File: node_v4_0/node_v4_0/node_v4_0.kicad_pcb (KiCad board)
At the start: 4 copper layers, 45.7 x 76.2 mm, 51 parts, among them J1 Conn_01x02_Pin, J2 12402012E212A, Q1 DMG2301L, U1 RP2040, U2 W25Q128JVS, U3 AP2112K-3.3, U4 CAT3200-5, U5 MCP73831-2-OT, U6 RFM69HCW, U7 PTS526 SK15 SMTR2 LFS, U8 PTS526 SK15 SMTR2 LFS

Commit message: minor
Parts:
- moved Q1 26.1 mm to (136.6, 85.9), turned to 180 degrees
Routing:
- net +BATT: track 50.3 -> 56.6 mm, vias 1 -> 2
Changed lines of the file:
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@@
 		(at 116.701 53.543 180)
 		(property "Reference" "J2"
-			(at -1.62 -8.405 360)
+			(at -1.62 -8.405 0)
 			(layer "F.SilkS")
 			(effects
@@
 		)
 		(property "Value" "12402012E212A"
-			(at 9.175 -6.715 360)
+			(at 9.175 -6.715 0)
 			(layer "F.Fab")
 			(effects
@@
 		)
 		(property "Footprint" "usbc:AMPHENOL_12402012E212A"
-			(at 0 0 360)
+			(at 0 0 0)
 			(layer "F.Fab")
 			(hide yes)
@@
 		)
 		(property "Datasheet" ""
-			(at 0 0 360)
+			(at 0 0 0)
 			(layer "F.Fab")
 			(hide yes)
@@
 		)
 		(property "Description" ""
-			(at 0 0 360)
+			(at 0 0 0)
 			(layer "F.Fab")
 			(hide yes)
@@
 		(tags "resistor handsolder")
 		(property "Reference" "R7"
-			(at 0 -1.65 360)
+			(at 0 -1.65 0)
 			(layer "F.SilkS")
 			(hide yes)
@@
 		)
 		(property "Value" "R"
-			(at 0 1.65 360)
+			(at 0 1.65 0)
 			(layer "F.Fab")
 			(effects
@@
 		)
 		(fp_text user "${REFERENCE}"
-			(at 0 0 360)
+			(at 0 0 0)
 			(layer "F.Fab")
 			(effects
@@
 	(footprint "Package_TO_SOT_SMD:SOT-23"
 		(layer "F.Cu")
-		(at 160.0985 74.676)
+		(at 136.5735 85.918 180)
 		(descr "SOT, 3 Pin (https://www.jedec.org/system/files/docs/to-236h.pdf variant AB), generated with kicad-footprint-generator ipc_gullwing_generator.py")
 		(tags "SOT TO_SOT_SMD")
 		(property "Reference" "Q1"
-			(at 0 -2.4 0)
+			(at 0 -2.4 360)
 			(layer "F.SilkS")
 			(effects
@@
 		)
 		(property "Value" "DMG2301L"
-			(at 0 2.4 0)
+			(at 0 2.4 360)
 			(layer "F.Fab")
 			(effects
@@
 		)
 		(property "Footprint" "Package_TO_SOT_SMD:SOT-23"
-			(at 0 0 0)
+			(at 0 0 180)
 			(unlocked yes)
 			(layer "F.Fab")
@@
 		)
 		(property "Datasheet" "https://www.diodes.com/assets/Datasheets/DMG2301L.pdf"
-			(at 0 0 0)
+			(at 0 0 180)
 			(unlocked yes)
 			(layer "F.Fab")
@@
 		)
 		(property "Description" "-3A Id, -20V Vds, P-Channel MOSFET, SOT-23"
-			(at 0 0 0)
+			(at 0 0 180)
 			(unlocked yes)
 			(layer "F.Fab")
@@
 		(attr smd)
 		(fp_line
-			(start 0 -1.56)
-			(end -0.65 -1.56)
+			(start 0 1.56)
+			(end 0.65 1.56)
 			(stroke
 				(width 0.12)
@@
 		)
 		(fp_line
-			(start 0 -1.56)
-			(end 0.65 -1.56)
+			(start 0 1.56)
+			(end -0.65 1.56)
 			(stroke
 				(width 0.12)
@@
 		)
 		(fp_line
-			(start 0 1.56)
-			(end -0.65 1.56)
+			(start 0 -1.56)
+			(end 0.65 -1.56)
 			(stroke
 				(width 0.12)
@@
 		)
 		(fp_line
-			(start 0 1.56)
-			(end 0.65 1.56)
+			(start 0 -1.56)
+			(end -0.65 -1.56)
 			(stroke
 				(width 0.12)
@@
 		)
 		(fp_line
-			(start -1.92 -1.7)
-			(end -1.92 1.7)
+			(start 1.92 1.7)
+			(end 1.92 -1.7)
 			(stroke
 				(width 0.05)
@@
 		)
 		(fp_line
-			(start -1.92 1.7)
-			(end 1.92 1.7)
+			(start 1.92 -1.7)
+			(end -1.92 -1.7)
 			(stroke
 				(width 0.05)
@@
 		)
 		(fp_line
-			(start 1.92 -1.7)
-			(end -1.92 -1.7)
+			(start -1.92 1.7)
+			(end 1.92 1.7)
 			(stroke
 				(width 0.05)
@@
 		)
 		(fp_line
-			(start 1.92 1.7)
-			(end 1.92 -1.7)
+			(start -1.92 -1.7)
+			(end -1.92 1.7)
 			(stroke
 				(width 0.05)
@@
 		)
 		(fp_line
-			(start -0.65 -1.125)
-			(end -0.325 -1.45)
+			(start 0.65 1.45)
+			(end -0.65 1.45)
 			(stroke
 				(width 0.1)
@@
 		)
 		(fp_line
-			(start -0.65 1.45)
-			(end -0.65 -1.125)
+			(start 0.65 -1.45)
+			(end 0.65 1.45)
 			(stroke
 				(width 0.1)
@@
 		)
 		(fp_line
-			(start 0.65 -1.45)
-			(end 0.65 1.45)
+			(start -0.65 1.45)
+			(end -0.65 -1.125)
 			(stroke
 				(width 0.1)
@@
 		)
 		(fp_line
-			(start 0.65 1.45)
-			(end -0.65 1.45)
+			(start -0.65 -1.125)
+			(end -0.325 -1.45)
 			(stroke
 				(width 0.1)
@@
 		)
 		(fp_text user "${REFERENCE}"
-			(at 0 0 0)
+			(at 0 0 360)
 			(layer "F.Fab")
 			(effects
@@
 		)
 		(pad "1" smd roundrect
-			(at -0.9375 -0.95)
+			(at -0.9375 -0.95 180)
 			(size 1.475 0.6)
 			(layers "F.Cu" "F.Paste" "F.Mask")
@@
 		)
 		(pad "2" smd roundrect
-			(at -0.9375 0.95)
+			(at -0.9375 0.95 180)
 			(size 1.475 0.6)
 			(layers "F.Cu" "F.Paste" "F.Mask")
@@
 		)
 		(pad "3" smd roundrect
-			(at 0.9375 0)
+			(at 0.9375 0 180)
 			(size 1.475 0.6)
 			(layers "F.Cu" "F.Paste" "F.Mask")
@@
 	)
 	(segment
+		(start 134.686 85.918)
+		(end 134.112 85.344)
+		(width 0.508)
+		(layer "F.Cu")
+		(net 55)
+	)
+	(segment
+		(start 134.112 85.344)
+		(end 134.112 80.772)
+		(width 0.508)
+		(layer "F.Cu")
+		(net 55)
+	)
+	(segment
 		(start 136.9965 74.125)
 		(end 137.425 73.6965)
@@
 		(net 55)
 	)
+	(segment
+		(start 135.636 85.918)
+		(end 134.686 85.918)
+		(width 0.508)
+		(layer "F.Cu")
+		(net 55)
+	)
 	(via
 		(at 134.112 72.644)
@@
 		(layers "F.Cu" "B.Cu")
 		(net 55)
+	)
+	(via
+		(at 134.112 80.772)
+		(size 0.6)
+		(drill 0.3)
+		(layers "F.Cu" "B.Cu")
+		(net 55)

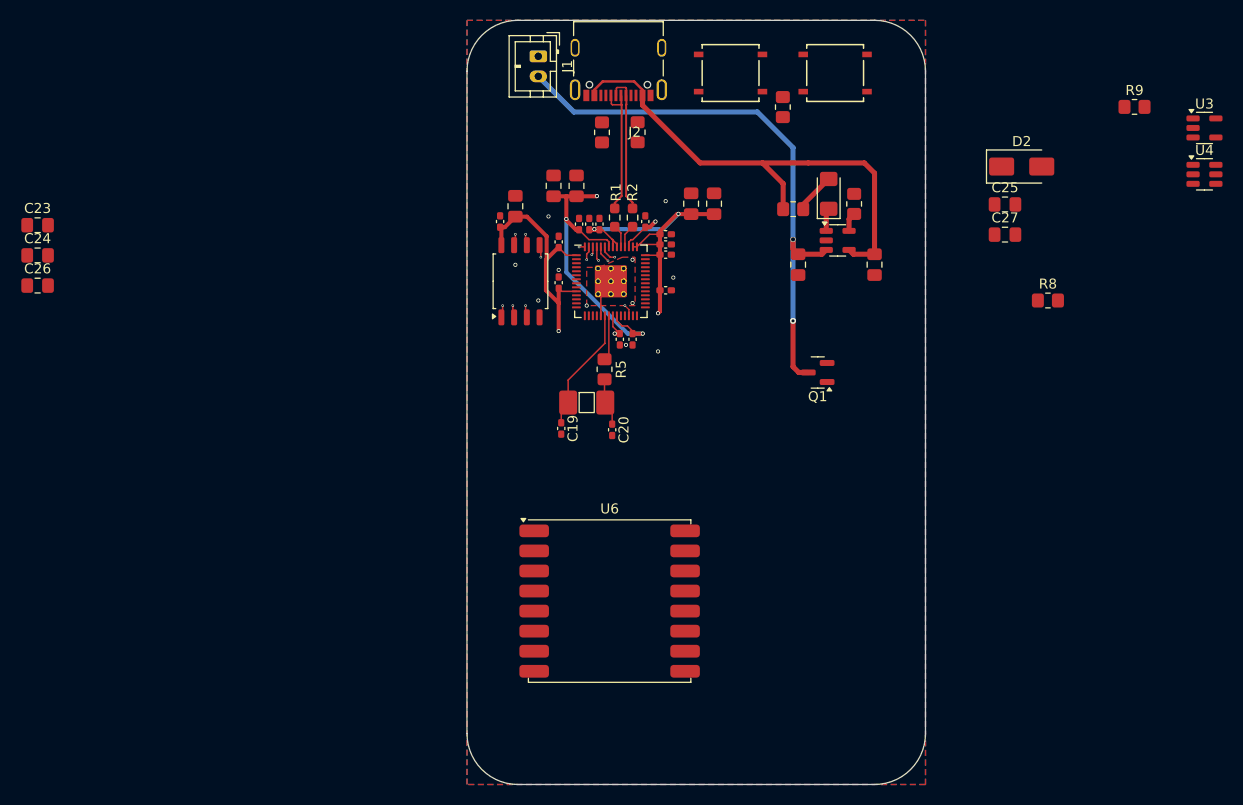
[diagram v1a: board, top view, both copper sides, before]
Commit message: more tracing, added RFM, added SIM, built power systems. converted to star ground
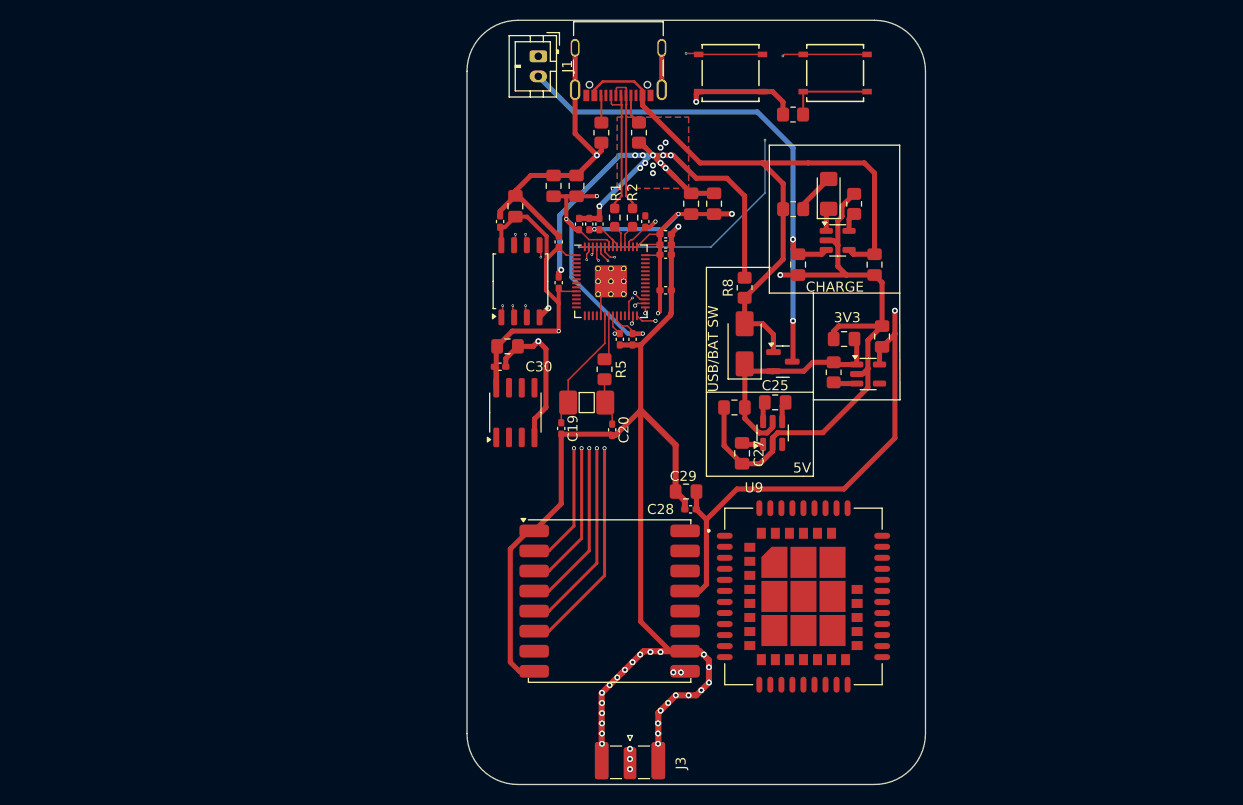
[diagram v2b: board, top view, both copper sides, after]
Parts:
- added C28: 0.1u, Capacitor_SMD:C_0402_1005Metric_Pad0.74x0.62mm_HandSolder, F.Cu at (123.9, 99.6)
- added C29: 10u, Capacitor_SMD:C_0805_2012Metric_Pad1.18x1.45mm_HandSolder, F.Cu at (123.4, 97.8)
- added C30: 0.1u, Capacitor_SMD:C_0402_1005Metric_Pad0.74x0.62mm_HandSolder, F.Cu at (104.9, 85.3)
- added C31: 10u, Capacitor_SMD:C_0805_2012Metric_Pad1.18x1.45mm_HandSolder, F.Cu at (105.6, 83.3)
- added J3: Conn_Coaxial, Connector_Coaxial:SMA_Samtec_SMA-J-P-H-ST-EM1_EdgeMount, F.Cu at (117.9, 124.9)
- added U10: MCP7940N-xP, Package_SO:SOIC-8_3.9x4.9mm_P1.27mm, F.Cu at (106.4, 89.9)
- added U9: SIM7080G, Library:XCVR_SIM7080G, F.Cu at (135.2, 108.2)
- moved C24 84.6 mm to (143.0, 82.3), turned to 90 degrees
- moved C23 81.2 mm to (139.2, 82.6), turned to 180 degrees
- moved C26 70.5 mm to (128.3, 89.4), turned to 180 degrees
- moved U4 50.2 mm to (132.1, 91.9), turned to 90 degrees
- moved U3 41.6 mm to (141.6, 86.1)
- moved R9 40.0 mm to (138.2, 85.9), turned to -90 degrees
- moved C27 34.1 mm to (129.0, 94.0), turned to -90 degrees
- moved D2 32.8 mm to (129.3, 83.1), turned to 90 degrees
- moved R8 30.3 mm to (129.3, 77.5), turned to 90 degrees
- moved C25 30.2 mm to (132.3, 88.9)
- moved R4 3.69 mm to (118.8, 62.0)
- moved Q1 3.64 mm to (133.1, 84.8), turned to 0 degrees
- moved R3 3.62 mm to (115.0, 62.0)
- moved R10 1.26 mm to (134.1, 60.2), turned to 180 degrees
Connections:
- J2 pad A5: unconnected-(J2-CC1_A-PadA5) -> Net-(J2-CC1_A)
- J2 pad A8: Net-(J2-SBU1) -> unconnected-(J2-SBU1-PadA8)
- J2 pad B5: unconnected-(J2-CC1_B-PadB5) -> Net-(J2-CC1_B)
- J2 pad B8: Net-(J2-SBU2) -> unconnected-(J2-SBU2-PadB8)
- J2 pad SH1: unconnected-(J2-SHIELD-PadSH1) -> GND
- J2 pad SH2: unconnected-(J2-SHIELD__1-PadSH2) -> GND
- J2 pad SH3: unconnected-(J2-SHIELD__2-PadSH3) -> GND
- J2 pad SH4: unconnected-(J2-SHIELD__3-PadSH4) -> GND
- R3 pad 1: Net-(J2-SBU1) -> Net-(J2-CC1_B)
- R4 pad 1: Net-(J2-SBU2) -> Net-(J2-CC1_A)
- U1 pad 27: unconnected-(U1-GPIO16-Pad27) -> MISO
- U1 pad 28: unconnected-(U1-GPIO17-Pad28) -> RFM_CS
- U1 pad 29: unconnected-(U1-GPIO18-Pad29) -> SPI_CK
- U1 pad 30: unconnected-(U1-GPIO19-Pad30) -> MOSI
- U1 pad 31: unconnected-(U1-GPIO20-Pad31) -> RFM_RST
- U6 pad 1: unconnected-(U6-GND-Pad1) -> GND
- U6 pad 10: unconnected-(U6-GND-Pad10) -> GND
- U6 pad 13: unconnected-(U6-3.3V-Pad13) -> +3.3V
- U6 pad 2: unconnected-(U6-MISO-Pad2) -> MISO
- U6 pad 3: unconnected-(U6-MOSI-Pad3) -> MOSI
- U6 pad 4: unconnected-(U6-SCK-Pad4) -> SPI_CK
- U6 pad 5: unconnected-(U6-NSS-Pad5) -> RFM_CS
- U6 pad 6: unconnected-(U6-RESET-Pad6) -> RFM_RST
- U6 pad 8: unconnected-(U6-GND-Pad8) -> GND
- U6 pad 9: unconnected-(U6-ANT-Pad9) -> /PERIPHERALS/ANT
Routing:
- net GND: track 2.28 -> 393.6 mm, vias 11 -> 45
- net +3.3V: track 73.3 -> 159.1 mm, vias 5 -> 7
- net /MCU/CS: track 11.8 -> 55.6 mm, vias 2 -> 4
- net RFM_RST: track 0.00 -> 43.1 mm, vias 0 -> 2
- net /MCU/RESET: track 1.18 -> 38.2 mm, vias 1 -> 2
- net RFM_CS: track 0.00 -> 36.9 mm, vias 0 -> 2
- net SPI_CK: track 0.00 -> 34.6 mm, vias 0 -> 2
- net MOSI: track 0.00 -> 32.8 mm, vias 0 -> 2
- net MISO: track 0.00 -> 30.4 mm, vias 0 -> 2
- net +VSW: track 0.00 -> 24.3 mm
- net VBUS: track 49.8 -> 67.9 mm
- net /PERIPHERALS/ANT: track 0.00 -> 13.4 mm, vias 0 -> 5
- net Net-(R10-Pad1): track 0.00 -> 8.84 mm
- net Net-(J2-CC1_A): track 0.00 -> 3.04 mm
- net Net-(J2-CC1_B): track 0.00 -> 2.73 mm
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- added copper zone on In1.Cu, net GND
- added copper zone on In2.Cu, net GND
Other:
- board text added: "3V3"
- board text added: "5V"
- board text added: "CHARGE"
- board text added: "USB/BAT SW"
